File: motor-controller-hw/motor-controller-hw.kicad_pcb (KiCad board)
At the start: 4 copper layers, 99.7 x 85.1 mm, 175 parts, among them J101 CAN, J102 Throttle, J103 Motor T, J104 Tran T, J105 USB_B_Micro, J106 Extra IO, J107 Hall Sensors, J108 CAN_DBG, J109 ABN Encoder, J110 SPI_DBG, J111 Trinamic-Bridge, J301 SWD, J302 User USART, J401 Trinamic_TRMI, J402 TMC4671 USART, Q101 Q_PMOS_GDS, SW301 Reset, SW302 Boot, SW303 User_SW, U101 AP7361C-33, U102 D36V6F5, U201 MCP6004, U202 MCP6004, U203 MCP6004, U204 74HC7014, U205 74HC7014, U206 mcp2562, U301 STM32F303RETx, U401 TMC4671, X401 IQXO-50, Y301 8Mhz

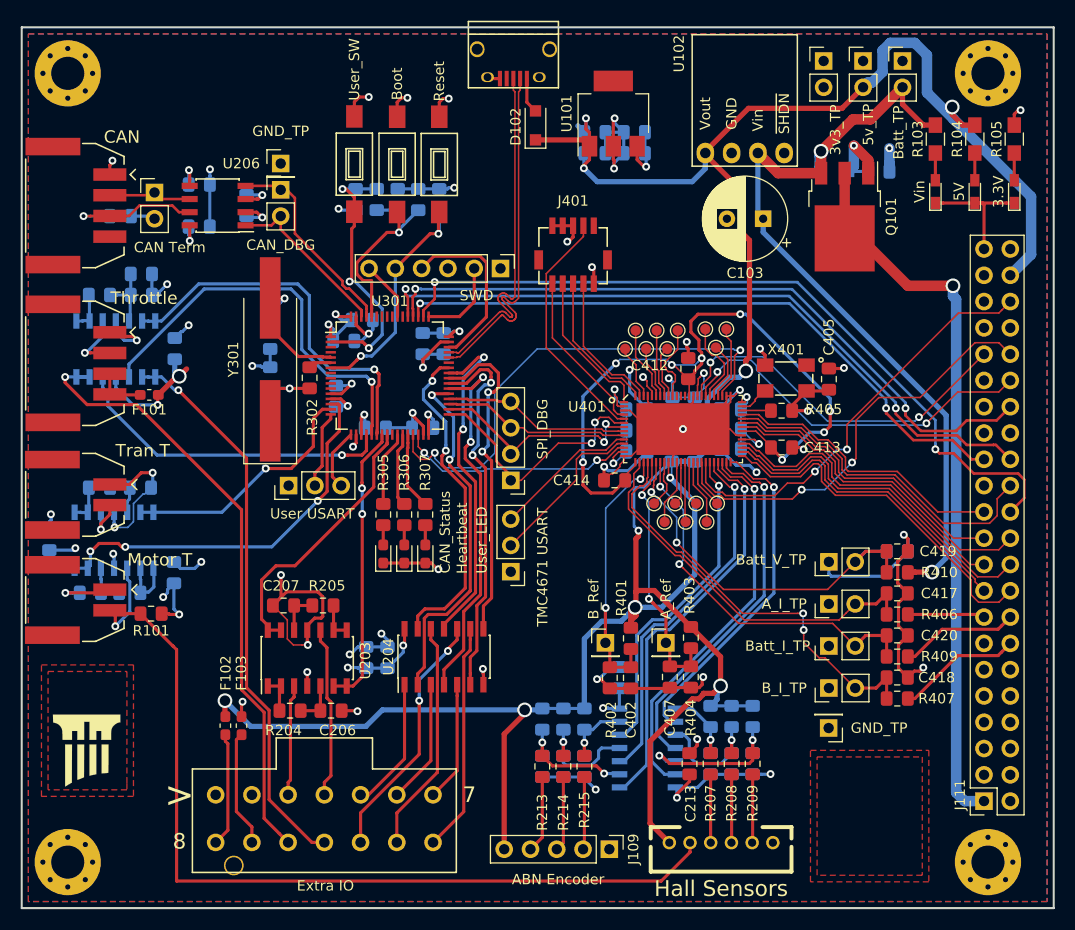
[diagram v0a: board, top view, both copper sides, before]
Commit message: PCB rev 1.1 -Fixed the TMC4671 footprint (use the Digi-Key layout) -Fixed the USB pull up issue for using the DFU bootloader -Fixed the orientation of the Hall sensor connector -Added a PTC on the hall effect sensor line -Added a 5v jumper for the CAN port
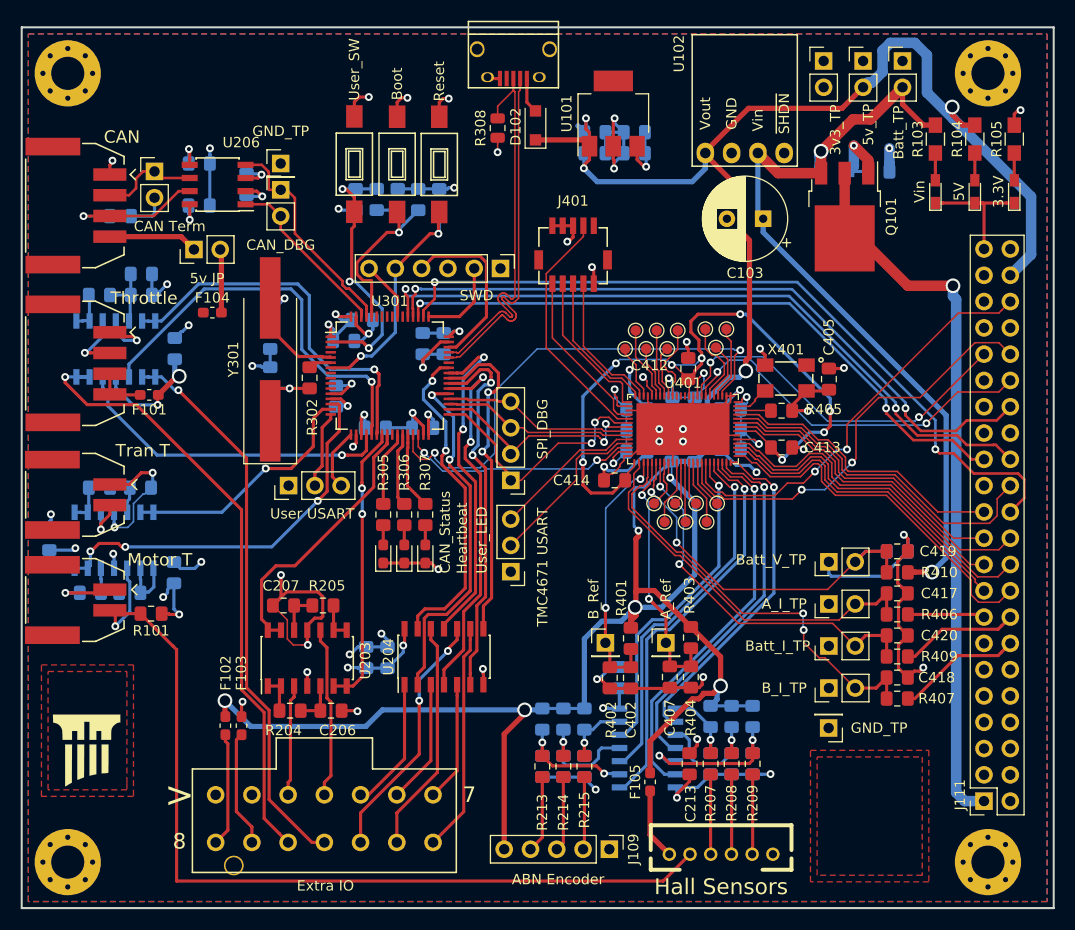
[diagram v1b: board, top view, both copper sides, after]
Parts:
- added F104: 120mA PTC, Fuse:Fuse_0603_1608Metric_Pad1.05x0.95mm_HandSolder, F.Cu at (61.0, 77.7)
- added F105: 50mA PTC, Fuse:Fuse_0603_1608Metric_Pad1.05x0.95mm_HandSolder, F.Cu at (103.3, 123.1)
- added JP101: 5v JP, Connector_PinHeader_2.54mm:PinHeader_1x02_P2.54mm_Vertical, F.Cu at (59.2, 71.6)
- added R308: 1K5, Resistor_SMD:R_0805_2012Metric, F.Cu at (88.5, 59.9)
- U401: footprint supermileage_footprints:TMC4671 -> supermileage_footprints:QFN76P
- moved JP201 2.03 mm to (55.4, 64.1)
- moved C212 2.03 mm to (59.7, 63.3)
- moved C202 2.03 mm to (64.3, 65.3)
- moved R220 2.03 mm to (59.7, 67.4)
- moved U206 2.03 mm to (61.5, 65.4)
- moved J107 1.12 mm to (110.1, 130.0), turned to 0 degrees
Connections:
- J107 pad 1: GNDD -> Net-(F105-Pad1)
- J107 pad 2: /HallC_in -> /MotorTemp
- J107 pad 3: /HallB_in -> /HallA_in
- J107 pad 4: /HallA_in -> /HallB_in
- J107 pad 5: /MotorTemp -> /HallC_in
- J107 pad 6: +5V -> GNDD
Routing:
- net +5V: track 287.7 -> 279.1 mm
- net Net-(J101-Pad4): track 0.00 -> 8.64 mm
- net Net-(F105-Pad1): track 0.00 -> 6.88 mm
- net Net-(F104-Pad2): track 0.00 -> 6.14 mm
- net /USB_D+: track 33.7 -> 38.2 mm
- net +3V3: track 108.2 -> 111.6 mm, vias 30 -> 31
- net /IO Protection/CAN_Rx: track 19.8 -> 22.2 mm
- net Net-(JP201-Pad2): track 2.38 -> 4.27 mm
- net /CAN_L: track 8.09 -> 9.86 mm
- net /HallC_in: track 6.61 -> 7.73 mm
- net /HallB_in: track 6.60 -> 7.72 mm
- net /HallA_in: track 6.60 -> 7.72 mm
- net /MotorTemp: track 90.1 -> 89.1 mm
- net /TMC4671/RTMI_MOSI: track 14.5 -> 15.1 mm
- net /TMC4671/SPI_MISO: track 18.2 -> 18.7 mm
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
